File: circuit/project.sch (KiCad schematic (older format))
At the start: 1 part

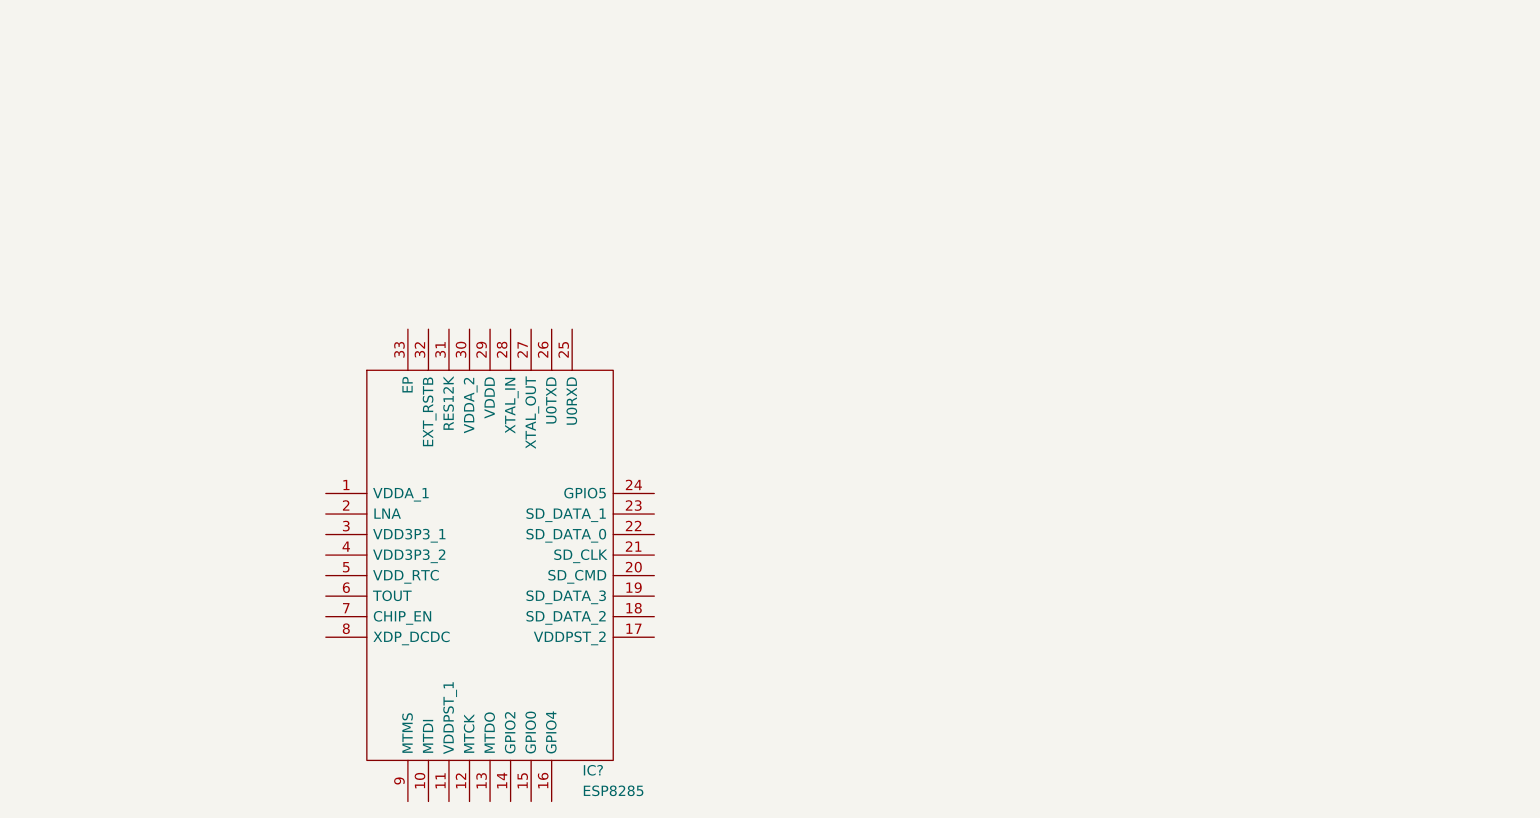
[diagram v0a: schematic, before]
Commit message: Add crystal to circuit
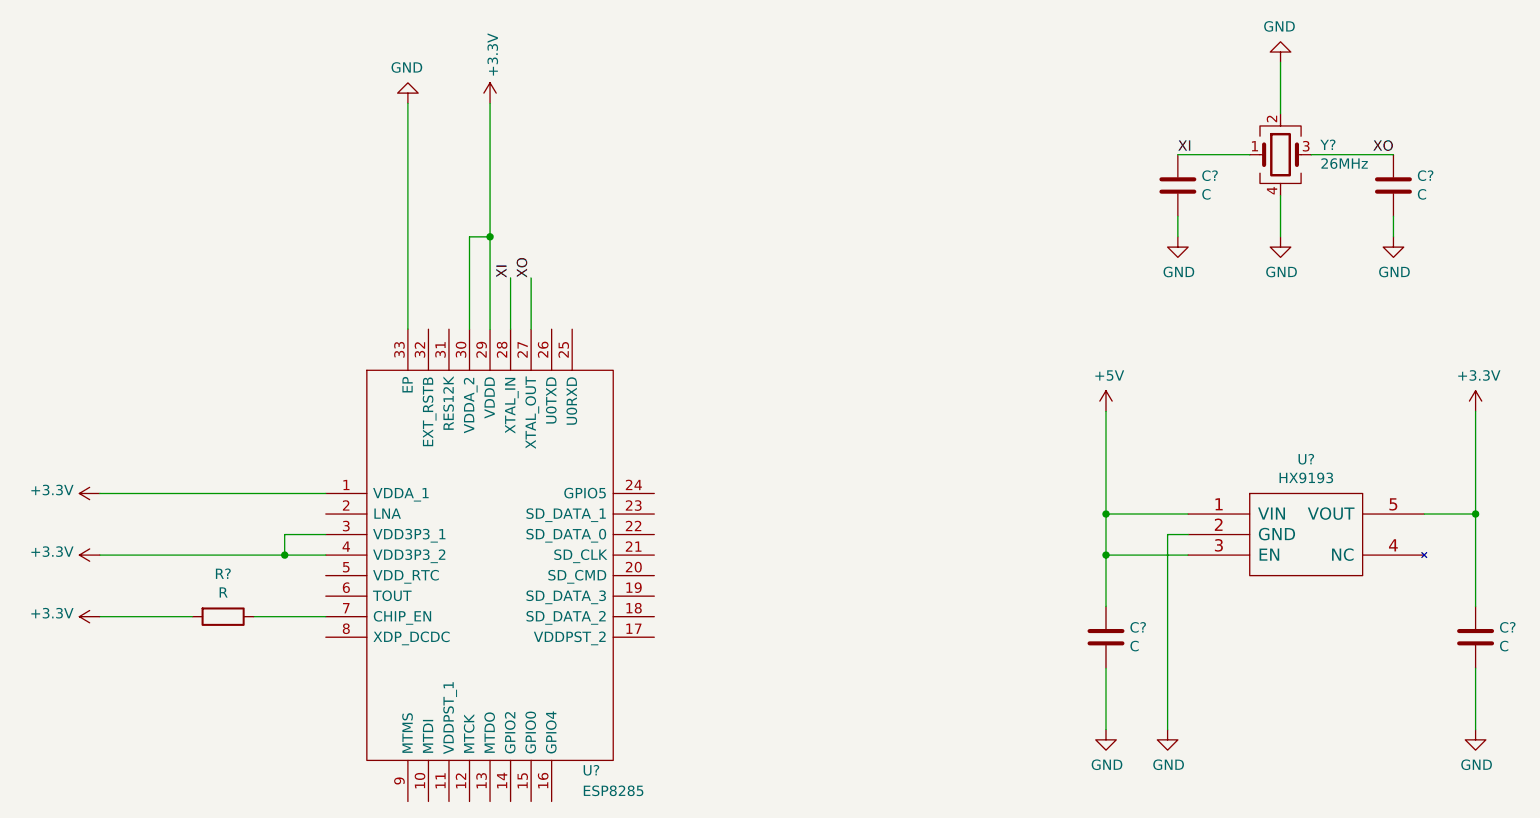
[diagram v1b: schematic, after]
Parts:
- added C? (x4): C, symbol Device:C
- added R?: R, symbol Device:R
- added U?: HX9193, Package_TO_SOT_SMD:SOT-23-5, symbol ESP8285:HX9193
- added Y?: 26MHz, Crystal:Crystal_SMD_3225-4Pin_3.2x2.5mm, symbol Device:Crystal_GND24
- U?: renamed from IC?; footprint QFN50P500X500X90-33N-D -> Package_DFN_QFN:QFN50P500X500X90-33N-D
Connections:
- net +3V3: now reaches U?.1 (VDDA_1)
- net +3V3: now also U?.29 (VDDD), U?.3 (VDD3P3_1), U?.30 (VDDA_2), U?.4 (VDD3P3_2), C?.1, R?.2, U?.5 (VOUT)
- net XO: now reaches U?.27 (XTAL_OUT)
- net XO: now also C?.1, Y?.3
- net XI: now reaches U?.28 (XTAL_IN)
- net XI: now also C?.1, Y?.1
- net GND: now reaches U?.33 (EP)
- net GND: now also C?.2, C?.2, C?.2, C?.2, U?.2 (GND), Y?.2, Y?.4
- net at U?.7 (CHIP_EN): now also R?.1
- new net +5V: C?.1, U?.1 (VIN), U?.3 (EN)

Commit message: Finished circuit design
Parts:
- added AE1: Antenna, symbol Device:Antenna
- added C1, C10, C11, C8, C9: 100nF, symbol Device:C
- added C12: C, symbol Device:C
- added C3: 2.4pF, symbol Device:C
- added C4: 3.0pF, symbol Device:C
- added D1, D2: LED, symbol Device:LED
- added J1: UART_CON, symbol Connector_Generic:Conn_01x03
- added J2: Conn_ARM_JTAG_SWD_20, symbol Connector:Conn_ARM_JTAG_SWD_20
- added L1: 2.2nH, symbol Device:L
- added P1: USB_C_Plug_USB2.0, symbol Connector:USB_C_Plug_USB2.0
- added R1, R2: 10kR, symbol Device:R
- added R4: 12kR, symbol Device:R
- added R5: 499R, symbol Device:R
- added R6, R7: 1kR, symbol Device:R
- added SW1, SW2: SW_DIP_x01, symbol Switch:SW_DIP_x01
- added U3: CH330N, Package_SO:SOIC-8_3.9x4.9mm_P1.27mm, symbol Interface_USB:CH330N
- C2, C5: renamed from C?; value C -> 100nF
- C6, C7: renamed from C?; value C -> 8pF
- R3: renamed from R?; value R -> 10kR
- gave numbers to parts that had none: 3
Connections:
- net +3V3: now also U2.11 (VDDPST_1), U2.17 (VDDPST_2), C10.1, C11.1, C8.1, C9.1, J2.1 (VTREF), J2.2 (VCC/NC), R1.2, R2.2
- net +5V: now also P1.A4 (VBUS), P1.A9 (VBUS), P1.B4 (VBUS), P1.B9 (VBUS), U3.5 (VCC)
- net GND: now also C1.2, C10.2, C11.2, C12.2, C3.2, C4.2, C8.2, C9.2, J1.1 (Pin_1), J2.10 (GND), J2.11 (RTCK), J2.12 (GND), J2.14 (GND), J2.16 (GND), J2.18 (GND), J2.20 (GND), J2.4 (GND), J2.6 (GND), J2.8 (GND), P1.A1 (GND), P1.A12 (GND), P1.B1 (GND), P1.B12 (GND), P1.S1 (SHIELD), R4.1, R6.2, R7.2, SW1.2, SW2.2, U3.3 (GND)
- net JTAG_TMS: now reaches U2.12 (MTCK)
- net JTAG_TMS: now also J2.7 (TMS/SWDIO)
- net LED_RUNNING: now reaches U2.13 (MTDO)
- net LED_RUNNING: now also D2.2 (A)
- net LED_CONNECTED: now reaches U2.14 (GPIO2)
- net LED_CONNECTED: now also D1.2 (A)
- net JTAG_nTRST: now reaches U2.15 (GPIO0)
- net JTAG_nTRST: now also J2.3 (~TRST~), R2.1, SW2.1
- net JTAG_TDI: now reaches U2.16 (GPIO4)
- net JTAG_TDI: now also J2.5 (TDI)
- net at U2.2 (LNA): now also C4.1, L1.2
- net JTAG_nRESET: now reaches U2.24 (GPIO5)
- net JTAG_nRESET: now also J2.15 (~SRST~)
- net U0_RXD: now reaches U2.25 (U0RXD)
- net U0_RXD: now also J1.2 (Pin_2), U3.6 (TXD)
- net at U2.26 (U0TXD): now also R5.1
- net at U2.31 (RES12K): now also R4.2
- net RST: now reaches U2.32 (EXT_RSTB)
- net RST: now also C1.1, R1.1, SW1.1
- net JTAG_TDO: now reaches U2.8 (XDP_DCDC)
- net JTAG_TDO: now also J2.13 (TDO/SWO)
- net JTAG_TCK: now reaches U2.9 (MTMS)
- net JTAG_TCK: now also J2.9 (TCK/SWDCLK)
- new net: AE1.1 (A), C3.1, L1.1
- new net: C12.1, U3.8 (V3)
- new net: D2.1 (K), R7.1
- new net: D1.1 (K), R6.1
- new net U0_TXD: J1.3 (Pin_3), R5.2, U3.7 (RXD)
- new net USB_DM: U3.2 (UD-)
- new net USB_DP: U3.1 (UD+)
- no-connect marks 0 -> 14
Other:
- moved on the sheet: C2, C5, C6, C7, R3, U1, U2, Y1

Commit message: finished PCB design
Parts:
- removed J1: UART_CON, symbol Connector_Generic:Conn_01x03
- removed J2: Conn_ARM_JTAG_SWD_20, symbol Connector:Conn_ARM_JTAG_SWD_20
- added J1: Conn_02x04_Odd_Even, Connector_PinHeader_1.27mm:PinHeader_2x04_P1.27mm_Vertical_SMD, symbol Connector_Generic:Conn_02x04_Odd_Even
- AE1: footprint (none) -> RF_Antenna:Johanson_2450AT18x100
- C1, C10, C11, C12, C2, C3, C4, C5, C6, C7, C8, C9: footprint (none) -> Capacitor_SMD:C_0603_1608Metric
- D1, D2: footprint (none) -> LED_SMD:LED_0603_1608Metric_Castellated
- L1: footprint (none) -> Inductor_SMD:L_0603_1608Metric
- P1: footprint (none) -> Connector_USB:USB_C_Receptacle_HRO_TYPE-C-31-M-12
- R1, R2, R3, R4, R5, R6, R7: footprint (none) -> Resistor_SMD:R_0603_1608Metric
- SW1, SW2: footprint (none) -> Button_Switch_SMD:SW_Push_SPST_NO_Alps_SKRK
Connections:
- net +3V3: now also J1.1 (Pin_1), J1.2 (Pin_2)
- net GND: now also J1.7 (Pin_7), J1.8 (Pin_8)
- net JTAG_TCK: now also J1.6 (Pin_6)
- net JTAG_TMS: now also J1.4 (Pin_4)
- net U0_RXD: now also J1.5 (Pin_5)
- net U0_TXD: now also J1.3 (Pin_3)
- net USB_DM: now also P1.A7 (D-), P1.B7 (D-)
- net USB_DP: now also P1.A6 (D+), P1.B6 (D+)
- no-connect marks 14 -> 12
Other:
- moved on the sheet: C12, D1, D2, P1, R6, R7, U3
